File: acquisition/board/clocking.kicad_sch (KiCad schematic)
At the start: 0 parts

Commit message: Continued initial design
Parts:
- added C1, C10, C11, C12, C2, C3, C4, C5, C6, C7, C8, C9: 0.1 uF, symbol device:C
- added R9: 100, symbol device:R
- added U11: LMK04806, symbol special-azonenberg:LMK04806
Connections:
- net CLK0_N: now also C2.2
- net CLK0_P: now also C1.2
- net CLK1_N: now also C8.2
- net CLK1_P: now also C7.2
- net CLK2_N: now also C4.2
- net CLK2_P: now also C3.2
- net CLK3_N: now also C10.2
- net CLK3_P: now also C9.2
- new net CLK0_AC_N: C2.1, U11.3 (CLKOUT1_N)
- new net CLK0_AC_P: C1.1, U11.4 (CLKOUT1_P)
- new net CLK1_AC_N: C8.1, U11.14 (CLKOUT2_N)
- new net CLK1_AC_P: C7.1, U11.13 (CLKOUT2_P)
- new net CLK2_AC_N: C4.1, U11.15 (CLKOUT3_N)
- new net CLK2_AC_P: C3.1, U11.16 (CLKOUT3_P)
- new net CLK3_AC_N: C10.1, U11.20 (CLKOUT4_N)
- new net CLK3_AC_P: C9.1, U11.19 (CLKOUT4_P)
- new net CLK5_AC_N: C6.1, U11.49 (CLKOUT6_N)
- new net CLK5_AC_P: C5.1, U11.48 (CLKOUT6_P)
- new net CLK_4: U11.22 (CLKOUT5_P)
- new net CLK_5_N: C6.2
- new net CLK_5_P: C5.2
- new net GND: U11.23 (GND), U11.PAD (GND)
- new net OSCIN_N: C12.2, R9.2, U11.37 (OSCIN_N)
- new net OSCIN_P: C11.2, R9.1, U11.36 (OSCIN_P)
- new net PLL_STATUS_CLKIN0: U11.62 (STATUS_CLKIN0)
- new net PLL_STATUS_CLKIN1: U11.63 (STATUS_CLKIN1)
- new net PLL_STATUS_HOLDOVER: U11.27 (STATUS_HOLDOVER)
- new net PLL_STATUS_LD: U11.33 (STATUS_LD)
- new net PLL_SYNC: U11.6 (SYNC)
- new net UWIRE_CLK: U11.45 (UWIRE_CLK)
- new net UWIRE_DATA: U11.46 (UWIRE_DATA)
- new net UWIRE_LE: U11.44 (UWIRE_LE)
- no-connect marks 0 -> 19
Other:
- note added: "CLK_[3:0] to ADCs: 10 MHz, LVDS CLK_4 to ice40: 10 MHz, LVCMOS18 CLK_5 to Artix: 100 MHz, LVDS"
- note added: "TODO: 100 MHz LVDS input clock"
- note added: "Use LMK04806, 2.5 GHz PLL VCO"
- company: (none) -> A. Zonenberg
- title: (none) -> Digitizer board

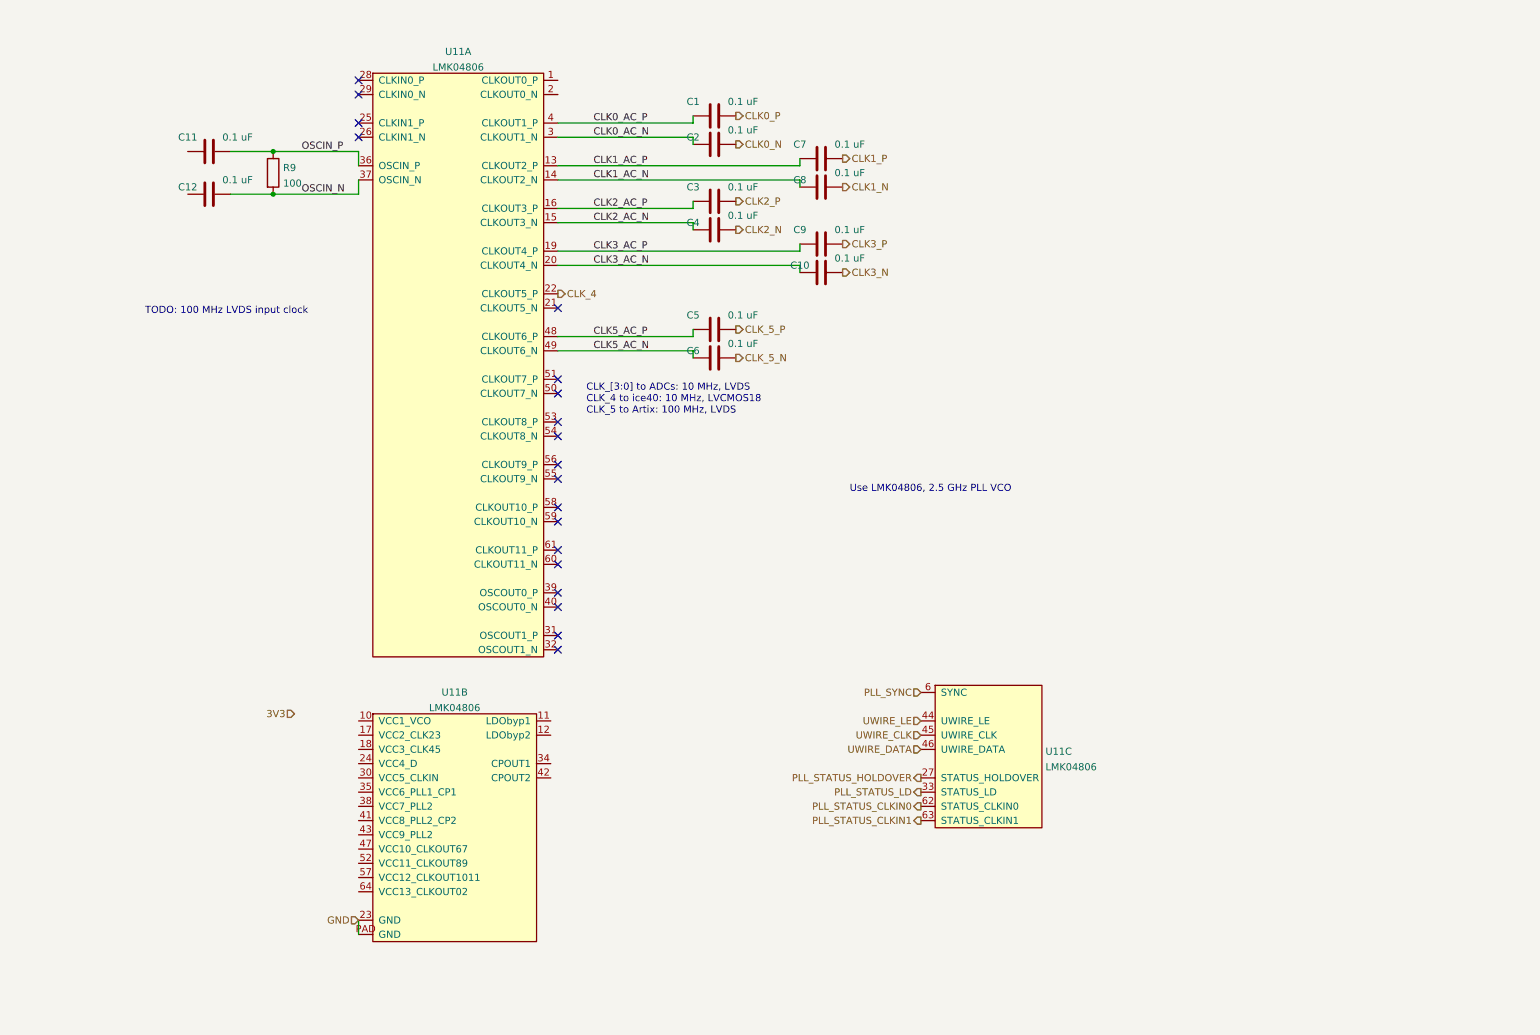
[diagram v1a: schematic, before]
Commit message: Updated schematic with a lot of level shifting and support stuff, power decoupling, etc. Almost done except power supply and protection diodes
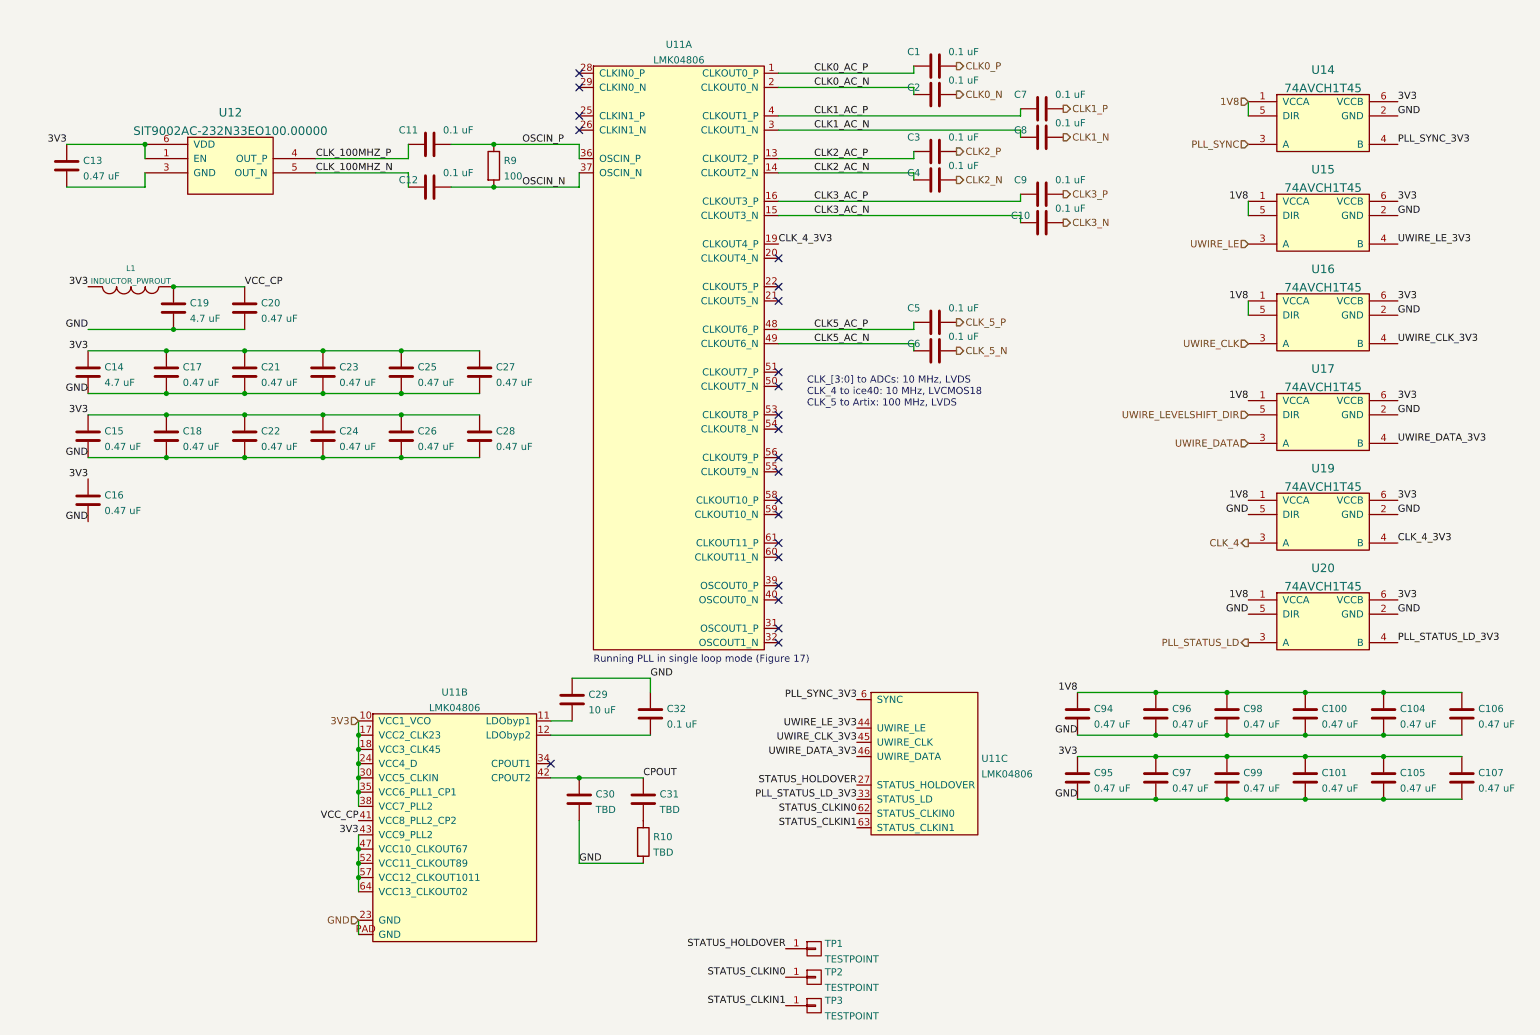
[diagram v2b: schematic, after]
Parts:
- added C100, C101, C104, C105, C106, C107, C13, C15, C16, C17, C18, C20, C21, C22, C23, C24, C25, C26, C27, C28, C94, C95, C96, C97, C98, C99: 0.47 uF, symbol device:C
- added C14, C19: 4.7 uF, symbol device:C
- added C29: 10 uF, symbol device:C
- added C30, C31: TBD, symbol device:C
- added C32: 0.1 uF, symbol device:C
- added L1: INDUCTOR_PWROUT, symbol passive-azonenberg:INDUCTOR_PWROUT
- added R10: TBD, symbol device:R
- added TP1, TP2, TP3: TESTPOINT, symbol conn:CONN_01X01
- added U12: SIT9002AC-232N33EO100.00000, symbol osc-azonenberg:OSC_LVDS_NOPAD
- added U14, U15, U16, U17, U19, U20: 74AVCH1T45, symbol special-azonenberg:74LVC1T45
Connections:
- net 3V3: now also U11.10 (VCC1_VCO), U11.17 (VCC2_CLK23), U11.18 (VCC3_CLK45), U11.24 (VCC4_D), U11.30 (VCC5_CLKIN), U11.35 (VCC6_PLL1_CP1), U11.38 (VCC7_PLL2), U11.43 (VCC9_PLL2), U11.47 (VCC10_CLKOUT67), U11.52 (VCC11_CLKOUT89), U11.57 (VCC12_CLKOUT1011), U11.64 (VCC13_CLKOUT02), C101.1, C105.1, C107.1, C13.1, C14.1, C15.1, C16.1, C17.1, C18.1, C21.1, C22.1, C23.1, C24.1, C25.1, C26.1, C27.1, C28.1, C95.1, C97.1, C99.1, L1.2, U12.1 (EN), U12.6 (VDD), U14.6 (VCCB), U15.6 (VCCB), U16.6 (VCCB), U17.6 (VCCB), U19.6 (VCCB), U20.6 (VCCB)
- net CLK0_AC_N: now also U11.2 (CLKOUT0_N); no longer U11.3 (CLKOUT1_N)
- net CLK0_AC_P: now also U11.1 (CLKOUT0_P); no longer U11.4 (CLKOUT1_P)
- net CLK1_AC_N: now also U11.3 (CLKOUT1_N); no longer U11.14 (CLKOUT2_N)
- net CLK1_AC_P: now also U11.4 (CLKOUT1_P); no longer U11.13 (CLKOUT2_P)
- net CLK2_AC_N: now also U11.14 (CLKOUT2_N); no longer U11.15 (CLKOUT3_N)
- net CLK2_AC_P: now also U11.13 (CLKOUT2_P); no longer U11.16 (CLKOUT3_P)
- net CLK3_AC_N: now also U11.15 (CLKOUT3_N); no longer U11.20 (CLKOUT4_N)
- net CLK3_AC_P: now also U11.16 (CLKOUT3_P); no longer U11.19 (CLKOUT4_P)
- net CLK_4: now also U19.3 (A); no longer U11.22 (CLKOUT5_P)
- net GND: now also C100.2, C101.2, C104.2, C105.2, C106.2, C107.2, C14.2, C15.2, C16.2, C17.2, C18.2, C19.2, C20.2, C21.2, C22.2, C23.2, C24.2, C25.2, C26.2, C27.2, C28.2, C29.1, C30.2, C32.1, C94.2, C95.2, C96.2, C97.2, C98.2, C99.2, R10.2, U14.2 (GND), U15.2 (GND), U16.2 (GND), U17.2 (GND), U19.2 (GND), U19.5 (DIR), U20.2 (GND), U20.5 (DIR)
- net PLL_STATUS_LD: now also U20.3 (A); no longer U11.33 (STATUS_LD)
- net PLL_SYNC: now also U14.3 (A); no longer U11.6 (SYNC)
- net UWIRE_CLK: now also U16.3 (A); no longer U11.45 (UWIRE_CLK)
- net UWIRE_DATA: now also U17.3 (A); no longer U11.46 (UWIRE_DATA)
- net UWIRE_LE: now also U15.3 (A); no longer U11.44 (UWIRE_LE)
- net CLK_100MHZ_N: now reaches C12.1
- net CLK_100MHZ_N: now also U12.5 (OUT_N)
- net at U11.11 (LDObyp1): now also C29.2
- net at U11.12 (LDObyp2): now also C32.2
- net VCC_CP: now reaches U11.41 (VCC8_PLL2_CP2)
- net VCC_CP: now also C19.1, C20.1, L1.1
- net CPOUT: now reaches U11.42 (CPOUT2)
- net CPOUT: now also C30.1, C31.1
- net CLK_100MHZ_P: now reaches C11.1
- net CLK_100MHZ_P: now also U12.4 (OUT_P)
- net PLL_STATUS_CLKIN0 renamed STATUS_CLKIN0
- net STATUS_CLKIN0: now also TP2.1 (P1)
- net PLL_STATUS_CLKIN1 renamed STATUS_CLKIN1
- net STATUS_CLKIN1: now also TP3.1 (P1)
- net PLL_STATUS_HOLDOVER renamed STATUS_HOLDOVER
- net STATUS_HOLDOVER: now also TP1.1 (P1)
- new net: C31.2, R10.1
- new net: C13.2, U12.3 (GND)
- new net 1V8: C100.1, C104.1, C106.1, C94.1, C96.1, C98.1, U14.1 (VCCA), U14.5 (DIR), U15.1 (VCCA), U15.5 (DIR), U16.1 (VCCA), U16.5 (DIR), U17.1 (VCCA), U19.1 (VCCA), U20.1 (VCCA)
- new net CLK_4_3V3: U11.19 (CLKOUT4_P), U19.4 (B)
- new net PLL_STATUS_LD_3V3: U11.33 (STATUS_LD), U20.4 (B)
- new net PLL_SYNC_3V3: U11.6 (SYNC), U14.4 (B)
- new net UWIRE_CLK_3V3: U11.45 (UWIRE_CLK), U16.4 (B)
- new net UWIRE_DATA_3V3: U11.46 (UWIRE_DATA), U17.4 (B)
- new net UWIRE_LEVELSHIFT_DIR: U17.5 (DIR)
- new net UWIRE_LE_3V3: U11.44 (UWIRE_LE), U15.4 (B)
- no-connect marks 19 -> 22
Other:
- note added: "Running PLL in single loop mode (Figure 17)"
- note removed: "TODO: 100 MHz LVDS input clock"
- note removed: "Use LMK04806, 2.5 GHz PLL VCO"
- moved on the sheet: C1, C10, C11, C12, C2, C3, C4, C5, C6, C7, C8, C9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
